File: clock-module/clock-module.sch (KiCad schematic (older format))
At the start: 6 parts

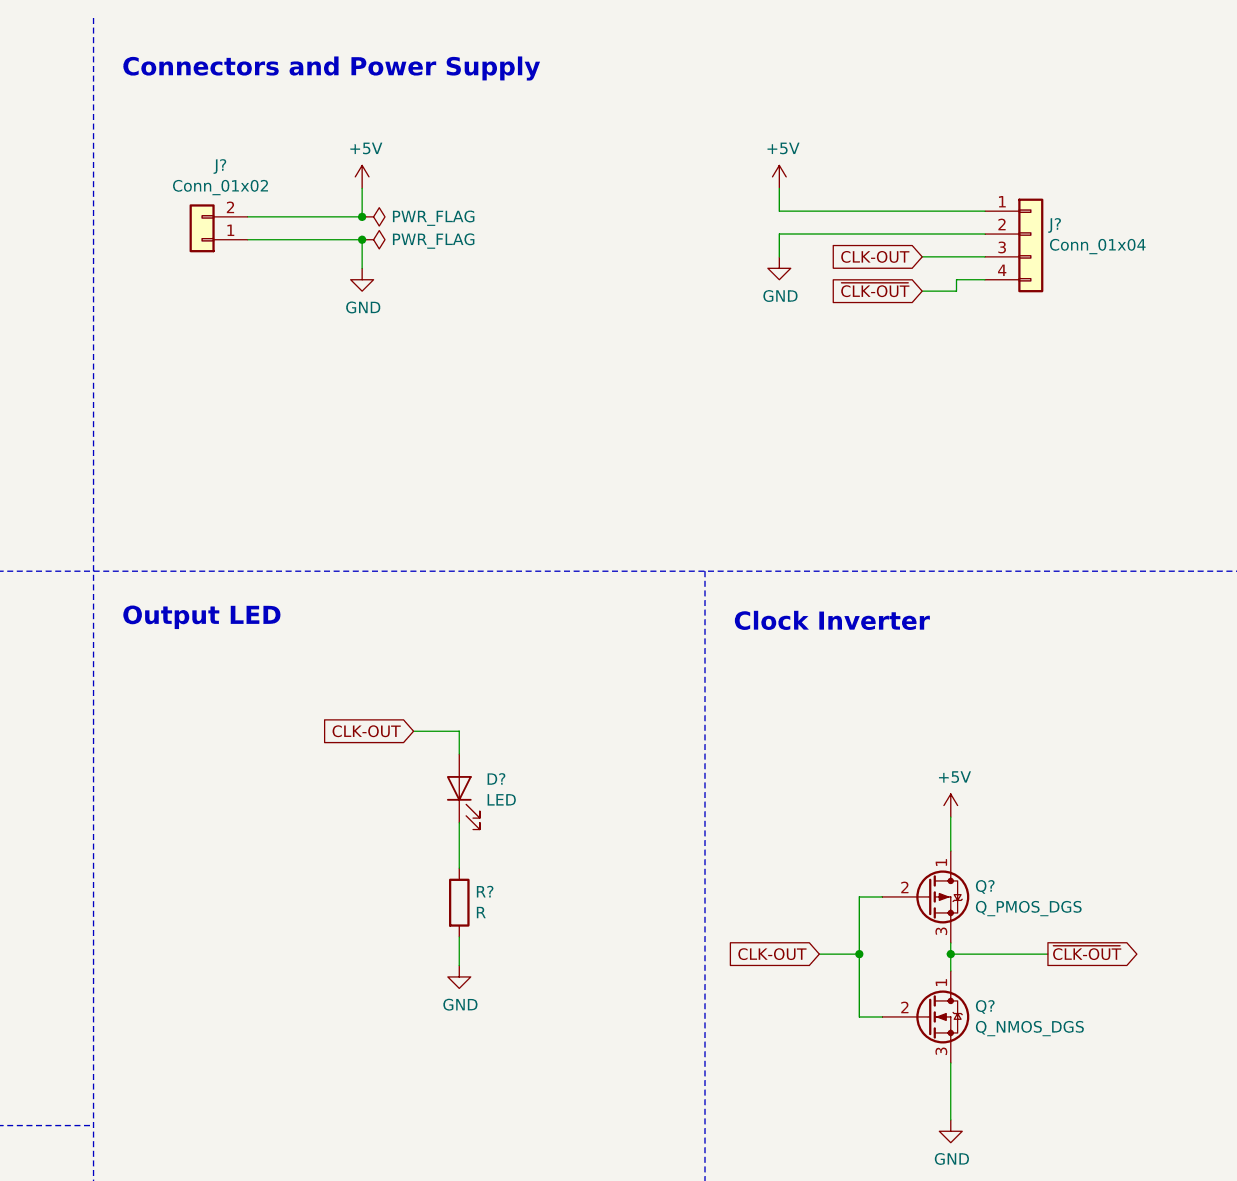
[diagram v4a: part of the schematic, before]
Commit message: ERC complete on clock-module, add HLT connector
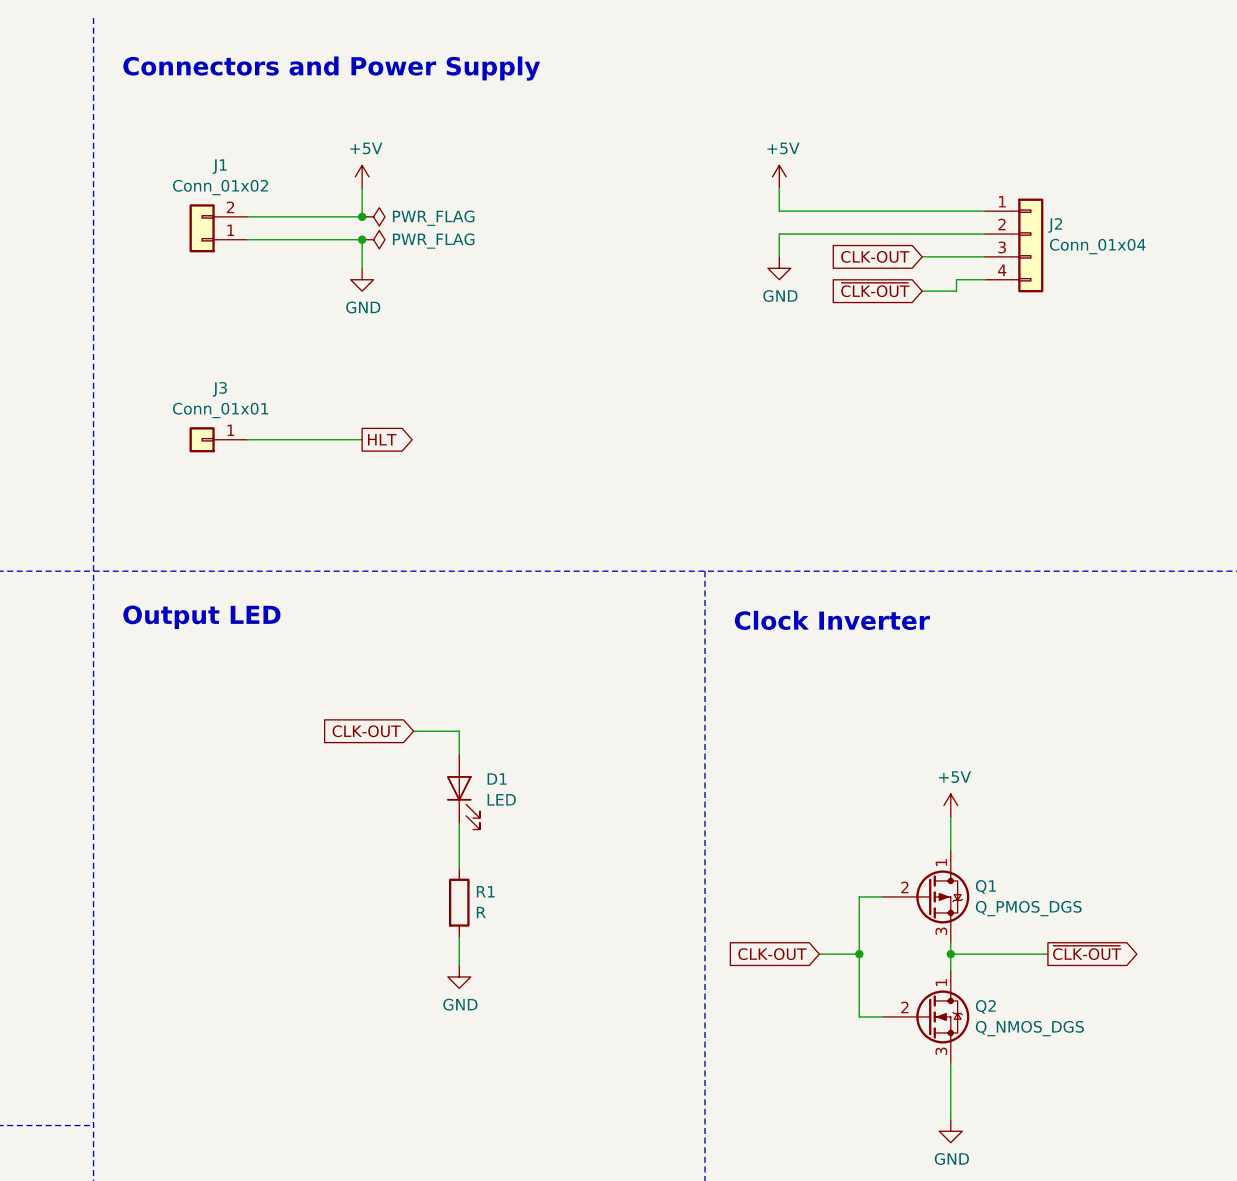
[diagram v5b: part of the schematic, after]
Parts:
- added J3: Conn_01x01, symbol Connector_Generic:Conn_01x01
- gave numbers to parts that had none: 6
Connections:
- new net HLT: J3.1 (Pin_1)
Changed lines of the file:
@@
 Connectors and Power Supply
 $Comp
-L Connector_Generic:Conn_01x02 J?
+L Connector_Generic:Conn_01x02 J1
 U 1 1 5D299965
 P 6325 1450
-F 0 "J?" H 6243 1125 50  0000 C CNN
+F 0 "J1" H 6243 1125 50  0000 C CNN
 F 1 "Conn_01x02" H 6243 1216 50  0000 C CNN
 F 2 "" H 6325 1450 50  0001 C CNN
@@
 $EndComp
 $Comp
-L power:+5V #PWR?
+L power:+5V #PWR0101
 U 1 1 5D29A606
 P 7025 1225
-F 0 "#PWR?" H 7025 1075 50  0001 C CNN
+F 0 "#PWR0101" H 7025 1075 50  0001 C CNN
 F 1 "+5V" H 7040 1398 50  0000 C CNN
 F 2 "" H 7025 1225 50  0001 C CNN
@@
 $EndComp
 $Comp
-L power:GND #PWR?
+L power:GND #PWR0102
 U 1 1 5D29B8C6
 P 7025 1575
-F 0 "#PWR?" H 7025 1325 50  0001 C CNN
+F 0 "#PWR0102" H 7025 1325 50  0001 C CNN
 F 1 "GND" H 7030 1402 50  0000 C CNN
 F 2 "" H 7025 1575 50  0001 C CNN
@@
 	7025 1450 7025 1575
 $Comp
-L power:PWR_FLAG #FLG?
+L power:PWR_FLAG #FLG0101
 U 1 1 5D29C6F5
 P 7025 1350
-F 0 "#FLG?" H 7025 1425 50  0001 C CNN
+F 0 "#FLG0101" H 7025 1425 50  0001 C CNN
 F 1 "PWR_FLAG" V 7025 1478 50  0000 L CNN
 F 2 "" H 7025 1350 50  0001 C CNN
@@
 Connection ~ 7025 1350
 $Comp
-L power:PWR_FLAG #FLG?
+L power:PWR_FLAG #FLG0102
 U 1 1 5D29CE65
 P 7025 1450
-F 0 "#FLG?" H 7025 1525 50  0001 C CNN
+F 0 "#FLG0102" H 7025 1525 50  0001 C CNN
 F 1 "PWR_FLAG" V 7025 1578 50  0000 L CNN
 F 2 "" H 7025 1450 50  0001 C CNN
@@
 Connection ~ 7025 1450
 $Comp
-L Connector_Generic:Conn_01x04 J?
+L Connector_Generic:Conn_01x04 J2
 U 1 1 5D29DA49
 P 9950 1425
-F 0 "J?" H 10030 1467 50  0000 L CNN
+F 0 "J2" H 10030 1467 50  0000 L CNN
 F 1 "Conn_01x04" H 10030 1376 50  0000 L CNN
 F 2 "" H 9950 1425 50  0001 C CNN
@@
 $EndComp
 $Comp
-L power:GND #PWR?
+L power:GND #PWR0103
 U 1 1 5D2A2021
 P 8850 1525
-F 0 "#PWR?" H 8850 1275 50  0001 C CNN
+F 0 "#PWR0103" H 8850 1275 50  0001 C CNN
 F 1 "GND" H 8855 1352 50  0000 C CNN
 F 2 "" H 8850 1525 50  0001 C CNN
@@
 $EndComp
 $Comp
-L power:+5V #PWR?
+L power:+5V #PWR0104
 U 1 1 5D2A294C
 P 8850 1225
-F 0 "#PWR?" H 8850 1075 50  0001 C CNN
+F 0 "#PWR0104" H 8850 1075 50  0001 C CNN
 F 1 "+5V" H 8865 1398 50  0000 C CNN
 F 2 "" H 8850 1225 50  0001 C CNN
@@
 CLK-OUT
 $Comp
-L Device:R R?
+L Device:R R1
 U 1 1 5D2B7458
 P 7450 4350
-F 0 "R?" H 7520 4396 50  0000 L CNN
+F 0 "R1" H 7520 4396 50  0000 L CNN
 F 1 "R" H 7520 4305 50  0000 L CNN
 F 2 "" V 7380 4350 50  0001 C CNN
@@
 $EndComp
 $Comp
-L Device:LED D?
+L Device:LED D1
 U 1 1 5D2B783D
 P 7450 3850
-F 0 "D?" V 7489 3733 50  0000 R CNN
+F 0 "D1" V 7489 3733 50  0000 R CNN
 F 1 "LED" V 7398 3733 50  0000 R CNN
 F 2 "" H 7450 3850 50  0001 C CNN
@@
 $EndComp
 $Comp
-L power:GND #PWR?
+L power:GND #PWR0105
 U 1 1 5D2B972F
 P 7450 4625
-F 0 "#PWR?" H 7450 4375 50  0001 C CNN
+F 0 "#PWR0105" H 7450 4375 50  0001 C CNN
 F 1 "GND" H 7455 4452 50  0000 C CNN
 F 2 "" H 7450 4625 50  0001 C CNN
@@
 CLK-OUT
 $Comp
-L Device:Q_NMOS_DGS Q?
+L Device:Q_NMOS_DGS Q2
 U 1 1 5D2BBA8E
 P 9500 4850
-F 0 "Q?" H 9706 4896 50  0000 L CNN
+F 0 "Q2" H 9706 4896 50  0000 L CNN
 F 1 "Q_NMOS_DGS" H 9706 4805 50  0000 L CNN
 F 2 "" H 9700 4950 50  0001 C CNN
@@
 $EndComp
 $Comp
-L Device:Q_PMOS_DGS Q?
+L Device:Q_PMOS_DGS Q1
 U 1 1 5D2BC068
 P 9500 4325
-F 0 "Q?" H 9706 4371 50  0000 L CNN
+F 0 "Q1" H 9706 4371 50  0000 L CNN
 F 1 "Q_PMOS_DGS" H 9706 4280 50  0000 L CNN
 F 2 "" H 9700 4425 50  0001 C CNN
@@
 $EndComp
 $Comp
-L power:GND #PWR?
+L power:GND #PWR0106
 U 1 1 5D2BD4A8
 P 9600 5300
-F 0 "#PWR?" H 9600 5050 50  0001 C CNN
+F 0 "#PWR0106" H 9600 5050 50  0001 C CNN
 F 1 "GND" H 9605 5127 50  0000 C CNN
 F 2 "" H 9600 5300 50  0001 C CNN
@@
 $EndComp
 $Comp
-L power:+5V #PWR?
+L power:+5V #PWR0107
 U 1 1 5D2BD8BB
 P 9600 3975
-F 0 "#PWR?" H 9600 3825 50  0001 C CNN
+F 0 "#PWR0107" H 9600 3825 50  0001 C CNN
 F 1 "+5V" H 9615 4148 50  0000 C CNN
 F 2 "" H 9600 3975 50  0001 C CNN
@@
 Wire Wire Line
 	9625 1625 9750 1625
+$Comp
+L Connector_Generic:Conn_01x01 J3
+U 1 1 5D691AB9
+P 6325 2325
+F 0 "J3" H 6243 2100 50  0000 C CNN
+F 1 "Conn_01x01" H 6243 2191 50  0000 C CNN
+F 2 "" H 6325 2325 50  0001 C CNN
+F 3 "~" H 6325 2325 50  0001 C CNN
+	1    6325 2325
+	-1   0    0    1
+$EndComp
+Text GLabel 7025 2325 2    50   Output ~ 0
+HLT
+Wire Wire Line
+	7025 2325 6525 2325
 $EndSCHEMATC
